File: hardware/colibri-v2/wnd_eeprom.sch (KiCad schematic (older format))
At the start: 2 parts

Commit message: Work on GPS. Added PCA9685
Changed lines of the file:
@@
 $Descr A4 11693 8268
 encoding utf-8
-Sheet 20 25
+Sheet 20 26
 Title ""
 Date ""
@@
 $EndComp
 Wire Wire Line
-	4850 2700 4850 3350
+	4850 2700 4850 3550
 Wire Wire Line
-	4850 3350 4850 3450
-Wire Wire Line
-	4850 3450 4850 3550
-Wire Wire Line
-	4400 3350 4850 3350
-Wire Wire Line
-	4850 3350 5100 3350
+	4400 3350 5100 3350
 Wire Wire Line
 	4850 3450 5100 3450

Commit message: work on wandboard service sheet.
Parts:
- U?: value BR24LFVJ-W -> BR24L02FVM-WTR
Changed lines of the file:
@@
 $Descr A4 11693 8268
 encoding utf-8
-Sheet 20 27
+Sheet 20 28
 Title ""
 Date ""
@@
 P 5550 3550
 F 0 "U?" H 5650 3900 60  0000 C CNN
-F 1 "BR24LFVJ-W" H 5550 3200 60  0000 C CNN
+F 1 "BR24L02FVM-WTR" H 5550 3200 60  0000 C CNN
 F 2 "Housings_SSOP:TSSOP-8_3x3mm_Pitch0.65mm" H 5550 3150 60  0001 C CNN
 F 3 "" H 5550 3450 60  0000 C CNN

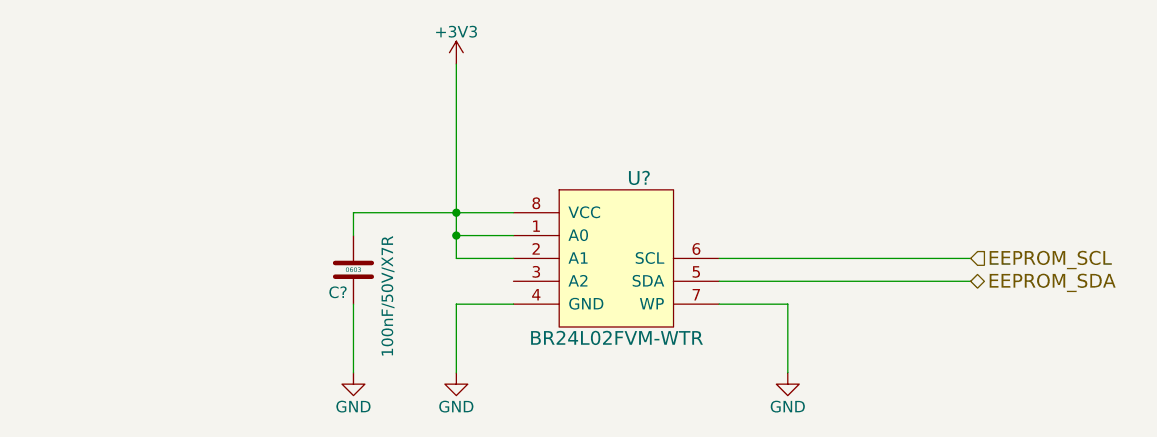
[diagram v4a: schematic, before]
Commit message: Resolving ERC problems
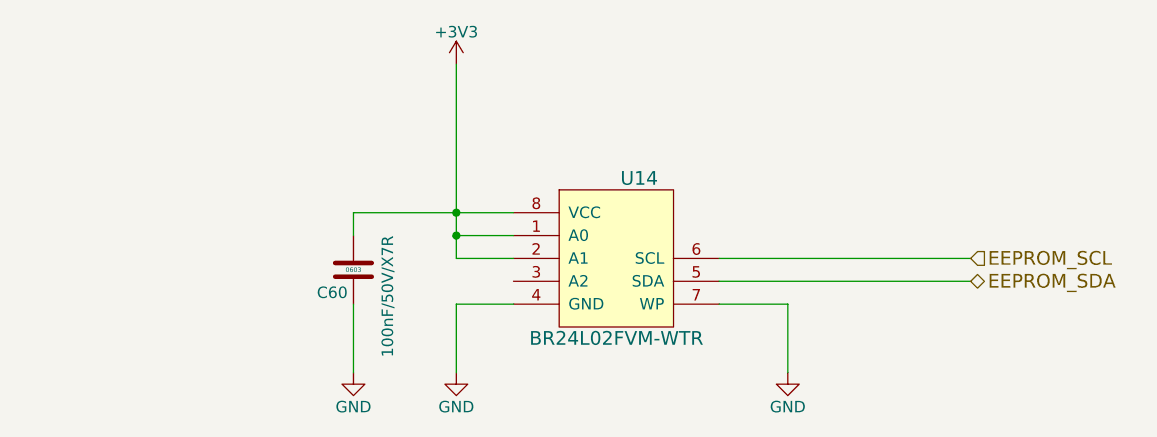
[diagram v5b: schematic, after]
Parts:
- gave numbers to parts that had none: 2
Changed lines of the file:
@@
 EESchema Schematic File Version 2
+LIBS:colibri-wnd-rescue
 LIBS:power
 LIBS:device
@@
 EEPROM_SCL
 $Comp
-L +3V3 #PWR?
+L +3V3 #PWR0168
 U 1 1 5669460C
 P 4850 2700
-F 0 "#PWR?" H 4850 2550 50  0001 C CNN
+F 0 "#PWR0168" H 4850 2550 50  0001 C CNN
 F 1 "+3V3" H 4850 2840 50  0000 C CNN
 F 2 "" H 4850 2700 50  0000 C CNN
@@
 Connection ~ 4850 3450
 $Comp
-L GND #PWR?
+L GND #PWR0169
 U 1 1 56694707
 P 4850 4050
-F 0 "#PWR?" H 4850 3800 50  0001 C CNN
+F 0 "#PWR0169" H 4850 3800 50  0001 C CNN
 F 1 "GND" H 4850 3900 50  0000 C CNN
 F 2 "" H 4850 4050 50  0000 C CNN
@@
 	4850 3750 4850 4050
 $Comp
-L GND #PWR?
+L GND #PWR0170
 U 1 1 566951C8
 P 6300 4050
-F 0 "#PWR?" H 6300 3800 50  0001 C CNN
+F 0 "#PWR0170" H 6300 3800 50  0001 C CNN
 F 1 "GND" H 6300 3900 50  0000 C CNN
 F 2 "" H 6300 4050 50  0000 C CNN
@@
 	6000 3650 7100 3650
 $Comp
-L C_SMT C?
+L C_SMT C60
 U 1 1 56695669
 P 4400 3600
-F 0 "C?" H 4425 3700 50  0000 L CNN
+F 0 "C60" H 4425 3700 50  0000 L CNN
 F 1 "100nF/50V/X7R" V 4250 3450 50  0000 L CNN
 F 2 "Capacitors_SMD:C_0603" H 4430 3450 30  0001 L CNN
@@
 $EndComp
 $Comp
-L BR24Lxxx-W U?
+L BR24Lxxx-W U14
 U 1 1 566962EE
 P 5550 3550
-F 0 "U?" H 5650 3900 60  0000 C CNN
+F 0 "U14" H 5650 3900 60  0000 C CNN
 F 1 "BR24L02FVM-WTR" H 5550 3200 60  0000 C CNN
 F 2 "Housings_SSOP:TSSOP-8_3x3mm_Pitch0.65mm" H 5550 3150 60  0001 C CNN
@@
 	4400 3350 4400 3450
 $Comp
-L GND #PWR?
+L GND #PWR0171
 U 1 1 5669653A
 P 4400 4050
-F 0 "#PWR?" H 4400 3800 50  0001 C CNN
+F 0 "#PWR0171" H 4400 3800 50  0001 C CNN
 F 1 "GND" H 4400 3900 50  0000 C CNN
 F 2 "" H 4400 4050 50  0000 C CNN

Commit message: Fixed ERC errors
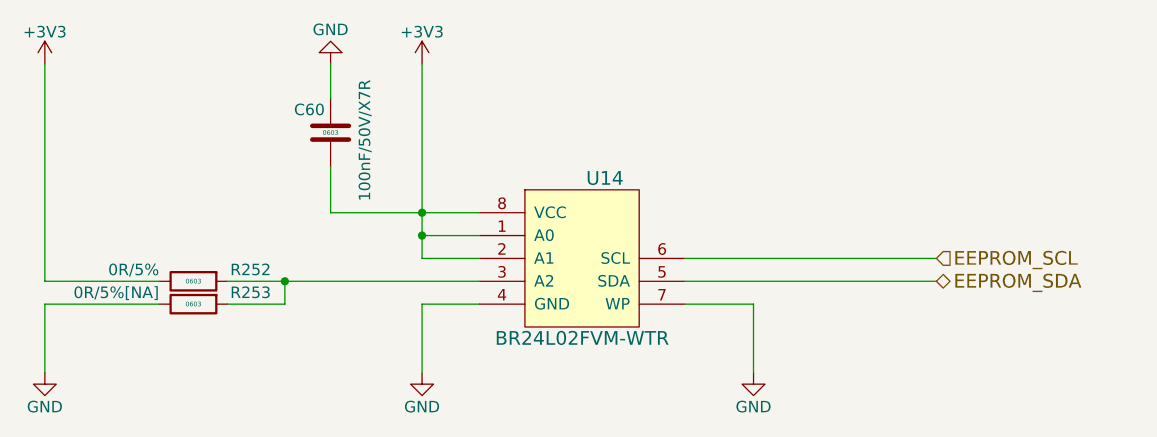
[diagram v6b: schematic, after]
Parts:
- added R252: 0R/5%, Resistors_SMD:R_0603, symbol R_SMT
- added R253: 0R/5%[NA], Resistors_SMD:R_0603, symbol R_SMT
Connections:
- net +3V3: now also R252.1
- net GND: now also R253.1
- net at U14.3 (A2): now also R252.2, R253.2
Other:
- moved on the sheet: C60, U14
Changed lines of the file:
@@
 $Descr A4 11693 8268
 encoding utf-8
-Sheet 19 28
+Sheet 18 28
 Title ""
 Date ""
@@
 Comment4 ""
 $EndDescr
-Text HLabel 7100 3650 2    60   BiDi ~ 0
+Text HLabel 6950 3650 2    60   BiDi ~ 0
 EEPROM_SDA
-Text HLabel 7100 3550 2    60   Input ~ 0
+Text HLabel 6950 3550 2    60   Input ~ 0
 EEPROM_SCL
 $Comp
-L +3V3 #PWR0168
+L +3V3 #PWR0172
 U 1 1 5669460C
-P 4850 2700
-F 0 "#PWR0168" H 4850 2550 50  0001 C CNN
-F 1 "+3V3" H 4850 2840 50  0000 C CNN
-F 2 "" H 4850 2700 50  0000 C CNN
-F 3 "" H 4850 2700 50  0000 C CNN
-	1    4850 2700
+P 4700 2700
+F 0 "#PWR0172" H 4700 2550 50  0001 C CNN
+F 1 "+3V3" H 4700 2840 50  0000 C CNN
+F 2 "" H 4700 2700 50  0000 C CNN
+F 3 "" H 4700 2700 50  0000 C CNN
+	1    4700 2700
 	1    0    0    -1
 $EndComp
 Wire Wire Line
-	4850 2700 4850 3550
+	4700 2700 4700 3550
 Wire Wire Line
-	4400 3350 5100 3350
+	4300 3350 4950 3350
 Wire Wire Line
-	4850 3450 5100 3450
-Connection ~ 4850 3350
+	4700 3450 4950 3450
+Connection ~ 4700 3350
 Wire Wire Line
-	4850 3550 5100 3550
-Connection ~ 4850 3450
+	4700 3550 4950 3550
+Connection ~ 4700 3450
 $Comp
-L GND #PWR0169
+L GND #PWR0173
 U 1 1 56694707
-P 4850 4050
-F 0 "#PWR0169" H 4850 3800 50  0001 C CNN
-F 1 "GND" H 4850 3900 50  0000 C CNN
-F 2 "" H 4850 4050 50  0000 C CNN
-F 3 "" H 4850 4050 50  0000 C CNN
-	1    4850 4050
+P 4700 4050
+F 0 "#PWR0173" H 4700 3800 50  0001 C CNN
+F 1 "GND" H 4700 3900 50  0000 C CNN
+F 2 "" H 4700 4050 50  0000 C CNN
+F 3 "" H 4700 4050 50  0000 C CNN
+	1    4700 4050
 	1    0    0    -1
 $EndComp
 Wire Wire Line
-	5100 3750 4850 3750
+	4950 3750 4700 3750
 Wire Wire Line
-	4850 3750 4850 4050
+	4700 3750 4700 4050
 $Comp
-L GND #PWR0170
+L GND #PWR0174
 U 1 1 566951C8
-P 6300 4050
-F 0 "#PWR0170" H 6300 3800 50  0001 C CNN
-F 1 "GND" H 6300 3900 50  0000 C CNN
-F 2 "" H 6300 4050 50  0000 C CNN
-F 3 "" H 6300 4050 50  0000 C CNN
-	1    6300 4050
+P 6150 4050
+F 0 "#PWR0174" H 6150 3800 50  0001 C CNN
+F 1 "GND" H 6150 3900 50  0000 C CNN
+F 2 "" H 6150 4050 50  0000 C CNN
+F 3 "" H 6150 4050 50  0000 C CNN
+	1    6150 4050
 	1    0    0    -1
 $EndComp
 Wire Wire Line
-	6000 3750 6300 3750
+	5850 3750 6150 3750
 Wire Wire Line
-	6300 3750 6300 4050
+	6150 3750 6150 4050
 Wire Wire Line
-	6000 3550 7100 3550
+	5850 3550 6950 3550
 Wire Wire Line
-	6000 3650 7100 3650
+	5850 3650 6950 3650
 $Comp
 L C_SMT C60
 U 1 1 56695669
-P 4400 3600
-F 0 "C60" H 4425 3700 50  0000 L CNN
-F 1 "100nF/50V/X7R" V 4250 3450 50  0000 L CNN
-F 2 "Capacitors_SMD:C_0603" H 4430 3450 30  0001 L CNN
-F 3 "" H 4425 3700 60  0000 L CNN
-F 4 "0603" H 4400 3600 20  0000 C CNN "SMT"
-F 5 "1414028" H 4430 3410 30  0001 L CNN "Part"
-F 6 "Farnell" H 4430 3370 30  0001 L CNN "Provider"
-	1    4400 3600
-	-1   0    0    1
+P 4300 3000
+F 0 "C60" H 4325 3100 50  0000 L CNN
+F 1 "100nF/50V/X7R" V 4150 2700 50  0000 L CNN
+F 2 "Capacitors_SMD:C_0603" H 4330 2850 30  0001 L CNN
+F 3 "" H 4325 3100 60  0000 L CNN
+F 4 "0603" H 4300 3000 20  0000 C CNN "SMT"
+F 5 "1414028" H 4330 2810 30  0001 L CNN "Part"
+F 6 "Farnell" H 4330 2770 30  0001 L CNN "Provider"
+	1    4300 3000
+	-1   0    0    -1
 $EndComp
 $Comp
 L BR24Lxxx-W U14
 U 1 1 566962EE
-P 5550 3550
-F 0 "U14" H 5650 3900 60  0000 C CNN
-F 1 "BR24L02FVM-WTR" H 5550 3200 60  0000 C CNN
-F 2 "Housings_SSOP:TSSOP-8_3x3mm_Pitch0.65mm" H 5550 3150 60  0001 C CNN
-F 3 "" H 5550 3450 60  0000 C CNN
-	1    5550 3550
+P 5400 3550
+F 0 "U14" H 5500 3900 60  0000 C CNN
+F 1 "BR24L02FVM-WTR" H 5400 3200 60  0000 C CNN
+F 2 "Housings_SSOP:TSSOP-8_3x3mm_Pitch0.65mm" H 5400 3150 60  0001 C CNN
+F 3 "" H 5400 3450 60  0000 C CNN
+	1    5400 3550
 	1    0    0    -1
 $EndComp
 Wire Wire Line
-	4400 3350 4400 3450
+	4300 3350 4300 3150
 $Comp
-L GND #PWR0171
+L GND #PWR0175
 U 1 1 5669653A
-P 4400 4050
-F 0 "#PWR0171" H 4400 3800 50  0001 C CNN
-F 1 "GND" H 4400 3900 50  0000 C CNN
-F 2 "" H 4400 4050 50  0000 C CNN
-F 3 "" H 4400 4050 50  0000 C CNN
-	1    4400 4050
+P 4300 2700
+F 0 "#PWR0175" H 4300 2450 50  0001 C CNN
+F 1 "GND" H 4300 2550 50  0000 C CNN
+F 2 "" H 4300 2700 50  0000 C CNN
+F 3 "" H 4300 2700 50  0000 C CNN
+	1    4300 2700
+	1    0    0    1
+$EndComp
+Wire Wire Line
+	4300 2850 4300 2700
+Wire Wire Line
+	3850 3750 4100 3750
+Wire Wire Line
+	3850 3650 4950 3650
+$Comp
+L R_SMT R253
+U 1 1 56CBB66B
+P 3700 3750
+F 0 "R253" V 3650 3500 50  0000 C CNN
+F 1 "0R/5%[NA]" V 3650 3900 50  0000 L CNN
+F 2 "Resistors_SMD:R_0603" V 3850 3750 30  0001 C CNN
+F 3 "" V 3780 3750 30  0000 C CNN
+F 4 "0603" V 3700 3750 20  0000 C CNN "SMT"
+F 5 "1469739" V 3900 3750 30  0001 C CNN "Part"
+F 6 "Farnell" V 3950 3750 30  0001 C CNN "Provider"
+	1    3700 3750
+	0    -1   1    0
+$EndComp
+$Comp
+L R_SMT R252
+U 1 1 56CBB675
+P 3700 3650
+F 0 "R252" V 3650 3400 50  0000 C CNN
+F 1 "0R/5%" V 3650 3800 50  0000 L CNN
+F 2 "Resistors_SMD:R_0603" V 3850 3650 30  0001 C CNN
+F 3 "" V 3780 3650 30  0000 C CNN
+F 4 "0603" V 3700 3650 20  0000 C CNN "SMT"
+F 5 "1469739" V 3900 3650 30  0001 C CNN "Part"
+F 6 "Farnell" V 3950 3650 30  0001 C CNN "Provider"
+	1    3700 3650
+	0    -1   1    0
+$EndComp
+$Comp
+L GND #PWR0176
+U 1 1 56CBB8F0
+P 3050 4050
+F 0 "#PWR0176" H 3050 3800 50  0001 C CNN
+F 1 "GND" H 3050 3900 50  0000 C CNN
+F 2 "" H 3050 4050 50  0000 C CNN
+F 3 "" H 3050 4050 50  0000 C CNN
+	1    3050 4050
+	1    0    0    -1
+$EndComp
+$Comp
+L +3V3 #PWR0177
+U 1 1 56CBB907
+P 3050 2700
+F 0 "#PWR0177" H 3050 2550 50  0001 C CNN
+F 1 "+3V3" H 3050 2840 50  0000 C CNN
+F 2 "" H 3050 2700 50  0000 C CNN
+F 3 "" H 3050 2700 50  0000 C CNN
+	1    3050 2700
 	1    0    0    -1
 $EndComp
 Wire Wire Line
-	4400 3750 4400 4050
+	3050 2700 3050 3650
+Wire Wire Line
+	3050 3650 3550 3650
+Wire Wire Line
+	3050 4050 3050 3750
+Wire Wire Line
+	3050 3750 3550 3750
+Wire Wire Line
+	4100 3750 4100 3650
+Connection ~ 4100 3650
 $EndSCHEMATC
